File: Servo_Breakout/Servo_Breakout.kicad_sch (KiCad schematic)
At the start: 14 parts, among them J101 395221002, J102 Conn_01x03, J103 Conn_01x04, Q101 2N7002, U101 TVS0500DRV

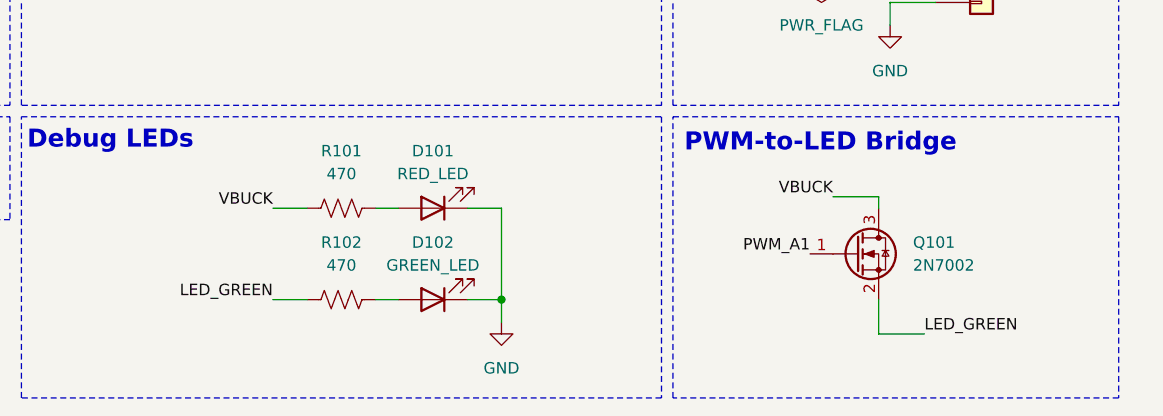
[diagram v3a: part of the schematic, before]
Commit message: completed layout rework for two 555 timers
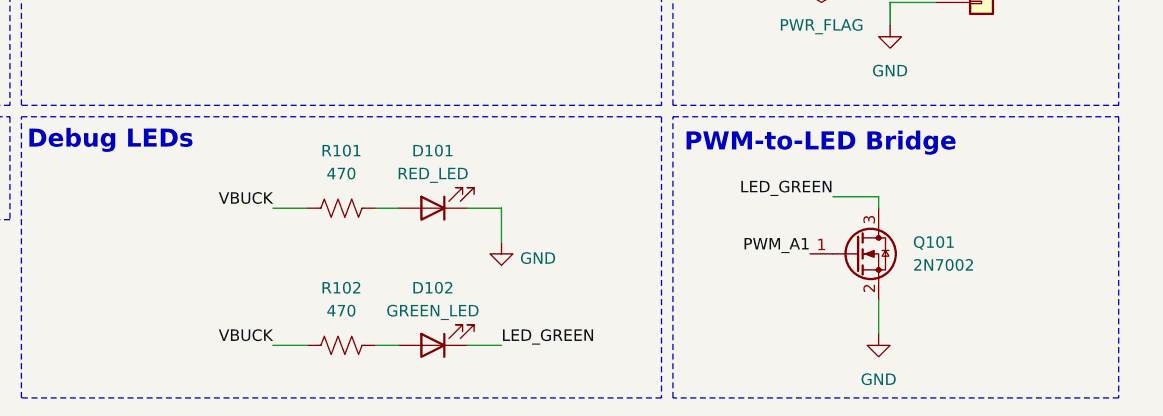
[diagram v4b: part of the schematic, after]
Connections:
- net GND: now also Q101.2 (S); no longer D102.1 (K)
- net LED_GREEN: now also D102.1 (K), Q101.3 (D); no longer Q101.2 (S), R102.1
- net VBUCK: now also R102.1; no longer Q101.3 (D)
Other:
- moved on the sheet: D102, R102
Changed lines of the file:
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@@
-	)
-	(junction
-		(at 172.72 130.81)
-		(diameter 0)
-		(color 0 0 0 0)
 	)
 	(junction
@@
 	(wire
 		(pts
-			(xy 172.72 130.81) (xy 172.72 133.35)
-		)
-		(stroke
-			(width 0)
-			(type default)
-		)
-	)
-	(wire
-		(pts
 			(xy 214.63 64.77) (xy 223.52 64.77)
 		)
@@
 	(wire
 		(pts
-			(xy 158.75 130.81) (xy 161.29 130.81)
+			(xy 158.75 135.89) (xy 161.29 135.89)
 		)
 		(stroke
@@
 	(wire
 		(pts
-			(xy 219.71 134.62) (xy 214.63 134.62)
+			(xy 172.72 120.65) (xy 172.72 124.46)
 		)
 		(stroke
@@
 	(wire
 		(pts
-			(xy 147.32 130.81) (xy 151.13 130.81)
+			(xy 147.32 135.89) (xy 151.13 135.89)
 		)
 		(stroke
@@
 	(wire
 		(pts
-			(xy 168.91 130.81) (xy 172.72 130.81)
+			(xy 168.91 135.89) (xy 172.72 135.89)
 		)
 		(stroke
@@
 		(pts
 			(xy 173.99 80.01) (xy 176.53 80.01)
-		)
-		(stroke
-			(width 0)
-			(type default)
-		)
-	)
-	(wire
-		(pts
-			(xy 172.72 120.65) (xy 172.72 130.81)
 		)
 		(stroke
@@
 		)
 	)
-	(label "LED_GREEN"
-		(at 147.32 130.81 180)
-		(effects
-			(font
-				(size 1.27 1.27)
-			)
-			(justify right bottom)
-		)
-	)
 	(label "I2C1_VCC"
 		(at 52.07 71.12 180)
@@
 		)
 	)
+	(label "LED_GREEN"
+		(at 172.72 135.89 0)
+		(effects
+			(font
+				(size 1.27 1.27)
+			)
+			(justify left bottom)
+		)
+	)
 	(label "VBUCK"
 		(at 147.32 120.65 180)
@@
 	)
 	(label "LED_GREEN"
-		(at 219.71 134.62 0)
-		(effects
-			(font
-				(size 1.27 1.27)
-			)
-			(justify left bottom)
+		(at 209.55 119.38 180)
+		(effects
+			(font
+				(size 1.27 1.27)
+			)
+			(justify right bottom)
 		)
 	)
@@
 		)
 	)
+	(label "VBUCK"
+		(at 147.32 135.89 180)
+		(effects
+			(font
+				(size 1.27 1.27)
+			)
+			(justify right bottom)
+		)
+	)
 	(label "PWM_A1"
 		(at 176.53 80.01 0)
@@
 	(label "PWM_A1"
 		(at 207.01 125.73 180)
-		(effects
-			(font
-				(size 1.27 1.27)
-			)
-			(justify right bottom)
-		)
-	)
-	(label "VBUCK"
-		(at 209.55 119.38 180)
 		(effects
 			(font
@@
 	)
 	(symbol
+		(lib_id "power:GND")
+		(at 214.63 134.62 0)
+		(unit 1)
+		(exclude_from_sim no)
+		(in_bom yes)
+		(on_board yes)
+		(dnp no)
+		(fields_autoplaced yes)
+		(property "Reference" "#PWR0109"
+			(at 214.63 140.97 0)
+			(effects
+				(font
+					(size 1.27 1.27)
+				)
+				(hide yes)
+			)
+		)
+		(property "Value" "GND"
+			(at 214.63 139.7 0)
+			(effects
+				(font
+					(size 1.27 1.27)
+				)
+			)
+		)
+		(property "Footprint" ""
+			(at 214.63 134.62 0)
+			(effects
+				(font
+					(size 1.27 1.27)
+				)
+				(hide yes)
+			)
+		)
+		(property "Datasheet" ""
+			(at 214.63 134.62 0)
+			(effects
+				(font
+					(size 1.27 1.27)
+				)
+				(hide yes)
+			)
+		)
+		(property "Description" "Power symbol creates a global label with name \"GND\" , ground"
+			(at 214.63 134.62 0)
+			(effects
+				(font
+					(size 1.27 1.27)
+				)
+				(hide yes)
+			)
+		)
+		(pin "1"
+		)
+		(instances
+			(project "Servo_Breakout"
+				(path "/d50da23a-d62e-4014-ae89-4f18c8c8c668"
+					(reference "#PWR0109")
+					(unit 1)
+				)
+			)
+		)
+	)
+	(symbol
 		(lib_id "Transistor_FET:2N7002")
 		(at 212.09 125.73 0)
@@
 	(symbol
 		(lib_id "Device:LED")
-		(at 165.1 130.81 180)
+		(at 165.1 135.89 180)
 		(unit 1)
 		(exclude_from_sim no)
@@
 		(dnp no)
 		(property "Reference" "D102"
-			(at 165.1 124.46 0)
+			(at 165.1 129.54 0)
 			(effects
 				(font
@@
 		)
 		(property "Value" "GREEN_LED"
-			(at 165.1 127 0)
+			(at 165.1 132.08 0)
 			(effects
 				(font
@@
 		)
 		(property "Footprint" "LED_SMD:LED_0603_1608Metric"
-			(at 165.1 130.81 0)
+			(at 165.1 135.89 0)
 			(effects
 				(font
@@
 		)
 		(property "Datasheet" "~"
-			(at 165.1 130.81 0)
+			(at 165.1 135.89 0)
 			(effects
 				(font
@@
 		)
 		(property "Description" "Light emitting diode"
-			(at 165.1 130.81 0)
+			(at 165.1 135.89 0)
 			(effects
 				(font
@@
 		)
 		(property "Sim.Pins" "1=K 2=A"
-			(at 165.1 130.81 0)
+			(at 165.1 135.89 0)
 			(effects
 				(font
@@
 	(symbol
 		(lib_id "power:GND")
-		(at 172.72 133.35 0)
+		(at 172.72 124.46 0)
 		(unit 1)
 		(exclude_from_sim no)
@@
 		(on_board yes)
 		(dnp no)
-		(fields_autoplaced yes)
 		(property "Reference" "#PWR0104"
-			(at 172.72 139.7 0)
+			(at 172.72 130.81 0)
 			(effects
 				(font
@@
 		)
 		(property "Value" "GND"
-			(at 172.72 138.43 0)
+			(at 176.784 126.238 0)
 			(effects
 				(font
@@
 		)
 		(property "Footprint" ""
-			(at 172.72 133.35 0)
+			(at 172.72 124.46 0)
 			(effects
 				(font
@@
 		)
 		(property "Datasheet" ""
-			(at 172.72 133.35 0)
+			(at 172.72 124.46 0)
 			(effects
 				(font
@@
 		)
 		(property "Description" "Power symbol creates a global label with name \"GND\" , ground"
-			(at 172.72 133.35 0)
+			(at 172.72 124.46 0)
 			(effects
 				(font
@@
 	(symbol
 		(lib_id "Device:R_US")
-		(at 154.94 130.81 90)
+		(at 154.94 135.89 90)
 		(unit 1)
 		(exclude_from_sim no)
@@
 		(dnp no)
 		(property "Reference" "R102"
-			(at 154.94 124.46 90)
+			(at 154.94 129.54 90)
 			(effects
 				(font
@@
 		)
 		(property "Value" "470"
-			(at 154.94 127 90)
+			(at 154.94 132.08 90)
 			(effects
 				(font
@@
 		)
 		(property "Footprint" "Resistor_SMD:R_0805_2012Metric_Pad1.20x1.40mm_HandSolder"
-			(at 155.194 129.794 90)
+			(at 155.194 134.874 90)
 			(effects
 				(font
@@
 		)
 		(property "Datasheet" "~"
-			(at 154.94 130.81 0)
+			(at 154.94 135.89 0)
 			(effects
 				(font
@@
 		)
 		(property "Description" "Resistor, US symbol"
-			(at 154.94 130.81 0)
-			(effects
-				(font
+			(at 154.94 135.89 0)
+			(effects
+				(font

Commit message: servo board final cleanup
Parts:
- removed R103, R104: 1k, Resistor_SMD:R_0805_2012Metric_Pad1.20x1.40mm_HandSolder, symbol Device:R_US
- J102: renamed from J103; footprint Connector_PinHeader_2.54mm:PinHeader_1x04_P2.54mm_Vertical -> Connector_PinHeader_2.54mm:PinHeader_1x05_P2.54mm_Vertical; symbol Connector_Generic:Conn_01x04 -> Connector_Generic:Conn_01x05
- renumbered J102 to J103
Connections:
- net CONN_I2C1_SCL: now also J102.2 (Pin_2)
- net CONN_I2C1_SDA: now also J102.3 (Pin_3)
- net GND: now also J102.5 (Pin_5); no longer J102.4 (Pin_4)
- net I2C1_VCC: now also J102.4 (Pin_4); no longer J102.3 (Pin_3)
- net SW_EN: now also J102.1 (Pin_1)
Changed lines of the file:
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@@
 	(wire
 		(pts
-			(xy 218.44 90.17) (xy 220.98 90.17)
+			(xy 208.28 90.17) (xy 220.98 90.17)
 		)
 		(stroke
@@
 	(wire
 		(pts
-			(xy 208.28 82.55) (xy 218.44 82.55)
-		)
-		(stroke
-			(width 0)
-			(type default)
-		)
-	)
-	(wire
-		(pts
 			(xy 52.07 71.12) (xy 55.88 71.12)
 		)
@@
 		(pts
 			(xy 214.63 134.62) (xy 214.63 130.81)
+		)
+		(stroke
+			(width 0)
+			(type default)
+		)
+	)
+	(wire
+		(pts
+			(xy 208.28 87.63) (xy 220.98 87.63)
 		)
 		(stroke
@@
 		)
 	)
+	(label "SW_EN"
+		(at 208.28 87.63 180)
+		(effects
+			(font
+				(size 1.27 1.27)
+			)
+			(justify right bottom)
+		)
+	)
 	(label "VBUCK"
 		(at 100.33 26.67 0)
@@
 	)
 	(label "CONN_I2C1_SDA"
-		(at 208.28 82.55 180)
+		(at 208.28 92.71 180)
 		(effects
 			(font
@@
 	)
 	(label "CONN_I2C1_SCL"
-		(at 208.28 85.09 180)
+		(at 208.28 90.17 180)
 		(effects
 			(font
@@
 	)
 	(symbol
-		(lib_id "Device:R_US")
-		(at 218.44 86.36 0)
-		(unit 1)
-		(exclude_from_sim no)
-		(in_bom yes)
-		(on_board yes)
-		(dnp no)
-		(fields_autoplaced yes)
-		(property "Reference" "R104"
-			(at 220.98 85.0899 0)
-			(effects
-				(font
-					(size 1.27 1.27)
-				)
-				(justify left)
-			)
-		)
-		(property "Value" "1k"
-			(at 220.98 87.6299 0)
-			(effects
-				(font
-					(size 1.27 1.27)
-				)
-				(justify left)
-			)
-		)
-		(property "Footprint" "Resistor_SMD:R_0805_2012Metric_Pad1.20x1.40mm_HandSolder"
-			(at 219.456 86.614 90)
-			(effects
-				(font
-					(size 1.27 1.27)
-				)
-				(hide yes)
-			)
-		)
-		(property "Datasheet" "~"
-			(at 218.44 86.36 0)
-			(effects
-				(font
-					(size 1.27 1.27)
-				)
-				(hide yes)
-			)
-		)
-		(property "Description" "Resistor, US symbol"
-			(at 218.44 86.36 0)
-			(effects
-				(font
-					(size 1.27 1.27)
-				)
-				(hide yes)
-			)
-		)
-		(pin "1"
-		)
-		(pin "2"
-		)
-		(instances
-			(project ""
-				(path "/d50da23a-d62e-4014-ae89-4f18c8c8c668"
-					(reference "R104")
-					(unit 1)
-				)
-			)
-		)
-	)
-	(symbol
 		(lib_id "Connector_Generic:Conn_01x03")
 		(at 228.6 64.77 0)
@@
 		(dnp no)
 		(fields_autoplaced yes)
-		(property "Reference" "J102"
+		(property "Reference" "J103"
 			(at 231.14 63.4999 0)
 			(effects
@@
 			(project ""
 				(path "/d50da23a-d62e-4014-ae89-4f18c8c8c668"
-					(reference "J102")
+					(reference "J103")
 					(unit 1)
 				)
@@
 		(dnp no)
 		(fields_autoplaced yes)
-		(property "Reference" "#PWR0109"
+		(property "Reference" "#PWR0106"
 			(at 214.63 140.97 0)
 			(effects
@@
 			(project "Servo_Breakout"
 				(path "/d50da23a-d62e-4014-ae89-4f18c8c8c668"
-					(reference "#PWR0109")
+					(reference "#PWR0106")
 					(unit 1)
 				)
@@
 	)
 	(symbol
-		(lib_id "Connector_Generic:Conn_01x04")
+		(lib_id "Connector_Generic:Conn_01x05")
 		(at 226.06 92.71 0)
 		(unit 1)
@@
 		(dnp no)
 		(fields_autoplaced yes)
-		(property "Reference" "J103"
-			(at 228.6 92.7099 0)
+		(property "Reference" "J102"
+			(at 228.6 91.4399 0)
 			(effects
 				(font
@@
 		)
 		(property "Value" "Conn_01x04"
-			(at 228.6 95.2499 0)
+			(at 228.6 93.9799 0)
 			(effects
 				(font
@@
 			)
 		)
-		(property "Footprint" "Connector_PinHeader_2.54mm:PinHeader_1x04_P2.54mm_Vertical"
+		(property "Footprint" "Connector_PinHeader_2.54mm:PinHeader_1x05_P2.54mm_Vertical"
 			(at 226.06 92.71 0)
 			(effects
@@
 			)
 		)
-		(property "Description" "Generic connector, single row, 01x04, script generated (kicad-library-utils/schlib/autogen/connector/)"
+		(property "Description" "Generic connector, single row, 01x05, script generated (kicad-library-utils/schlib/autogen/connector/)"
 			(at 226.06 92.71 0)
 			(effects
@@
 		(pin "3"
 		)
+		(pin "5"
+		)
 		(instances
 			(project ""
 				(path "/d50da23a-d62e-4014-ae89-4f18c8c8c668"
-					(reference "J103")
+					(reference "J102")
 					(unit 1)
 				)
@@
 	)
 	(symbol
-		(lib_id "Device:R_US")
-		(at 208.28 88.9 0)
-		(unit 1)
-		(exclude_from_sim no)
-		(in_bom yes)
-		(on_board yes)
-		(dnp no)
-		(fields_autoplaced yes)
-		(property "Reference" "R103"
-			(at 210.82 87.6299 0)
-			(effects
-				(font
-					(size 1.27 1.27)
-				)
-				(justify left)
-			)
-		)
-		(property "Value" "1k"
-			(at 210.82 90.1699 0)
-			(effects
-				(font
-					(size 1.27 1.27)
-				)
-				(justify left)
-			)
-		)
-		(property "Footprint" "Resistor_SMD:R_0805_2012Metric_Pad1.20x1.40mm_HandSolder"
-			(at 209.296 89.154 90)
-			(effects
-				(font
-					(size 1.27 1.27)
-				)
-				(hide yes)
-			)
-		)
-		(property "Datasheet" "~"
-			(at 208.28 88.9 0)
-			(effects
-				(font
-					(size 1.27 1.27)
-				)
-				(hide yes)
-			)
-		)
-		(property "Description" "Resistor, US symbol"
-			(at 208.28 88.9 0)
-			(effects
-				(font
-					(size 1.27 1.27)
-				)
-				(hide yes)
-			)
-		)
-		(pin "1"
-		)
-		(pin "2"
-		)
-		(instances
-			(project "Servo_Breakout"
-				(path "/d50da23a-d62e-4014-ae89-4f18c8c8c668"
-					(reference "R103")
-					(unit 1)
-				)
-			)
-		)
-	)
-	(symbol
 		(lib_id "power:GND")
 		(at 215.9 100.33 0)
@@
 		(dnp no)
 		(fields_autoplaced yes)
-		(property "Reference" "#PWR0106"
+		(property "Reference" "#PWR0107"
 			(at 215.9 106.68 0)
 			(effects
@@
 			(project "Servo_Breakout"
 				(path "/d50da23a-d62e-4014-ae89-4f18c8c8c668"
-					(reference "#PWR0106")
+					(reference "#PWR0107")
 					(unit 1)
 				)
@@
 			(project "Servo_Breakout"
 				(path "/d50da23a-d62e-4014-ae89-4f18c8c8c668"
-					(page "5")
+					(page "4")
 				)
 			)
@@
 			(project "Servo_Breakout"
 				(path "/d50da23a-d62e-4014-ae89-4f18c8c8c668"
-					(page "3")
+					(page "2")
 				)
 			)
@@
 			(project "Servo_Breakout"
 				(path "/d50da23a-d62e-4014-ae89-4f18c8c8c668"
-					(page "5")
-				)
-			)
+					(page "3")
+				)
+			)

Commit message: servo breakout gerbers
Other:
- company: (none) -> University of Illinois Urbana-Champaign
- title: (none) -> Servo Breakout
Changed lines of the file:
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@@
 	(generator_version "9.0")
 	(paper "A4")
+	(title_block
+		(title "Servo Breakout")
+		(date "2026-03-24")
+		(rev "A")
+		(company "University of Illinois Urbana-Champaign")
+		(comment 4 "Contributors: Noah Breit, Thomas McManamen")
+	)
 	(rectangle
 		(start 119.38 110.49)
